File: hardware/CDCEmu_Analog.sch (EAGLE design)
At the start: 72 parts, among them J1 Audio In, J2 Audio Out, J3 Mic In, Q1 PCH, Q10 NPN, Q2 NCH, Q3 NCH, Q4 PCH, Q5 NCH, Q6 NPN, Q7 NPN, Q8 NPN, Q9 NPN, U1 1117, U2 BK8000L, U3 LM358, U4 NE5532

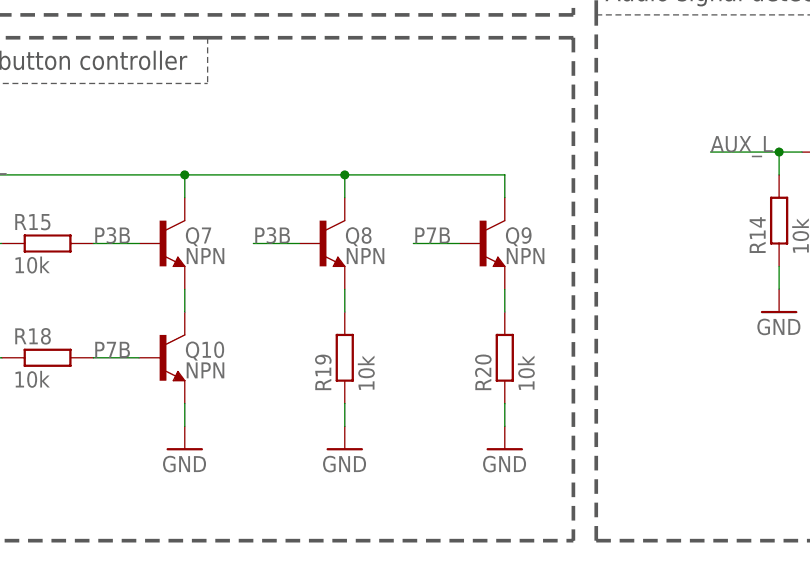
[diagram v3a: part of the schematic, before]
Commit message: [HW/Analog] Correct Vol+/- control transistors
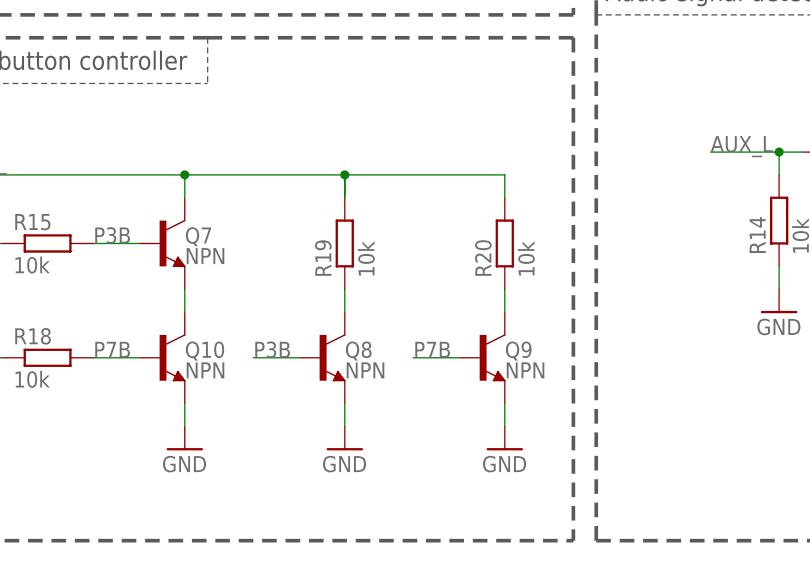
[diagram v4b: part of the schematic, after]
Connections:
- removed net Q7E: Q8.E, R19.2
- removed net Q8E: Q9.E, R20.2
- new net Q8C: Q8.C, R19.1
- new net Q9C: Q9.C, R20.1
- net CTRL: now also R19.2, R20.2; no longer Q8.C, Q9.C
- net GND: now also Q8.E, Q9.E; no longer R19.1, R20.1
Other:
- moved on the sheet: Q8, Q9, R19, R20
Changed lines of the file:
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@@
 <attribute name="VALUE" x="208.28" y="7.874" size="1.778" layer="96" font="vector"/>
 </instance>
-<instance part="Q8" gate="G$1" x="223.52" y="22.86" smashed="yes">
-<attribute name="NAME" x="226.06" y="22.86" size="1.778" layer="95" font="vector"/>
-<attribute name="VALUE" x="226.06" y="20.574" size="1.778" layer="96" font="vector"/>
-</instance>
-<instance part="Q9" gate="G$1" x="241.3" y="22.86" smashed="yes">
-<attribute name="NAME" x="243.84" y="22.86" size="1.778" layer="95" font="vector"/>
-<attribute name="VALUE" x="243.84" y="20.574" size="1.778" layer="96" font="vector"/>
+<instance part="Q8" gate="G$1" x="223.52" y="10.16" smashed="yes">
+<attribute name="NAME" x="226.06" y="10.16" size="1.778" layer="95" font="vector"/>
+<attribute name="VALUE" x="226.06" y="7.874" size="1.778" layer="96" font="vector"/>
+</instance>
+<instance part="Q9" gate="G$1" x="241.3" y="10.16" smashed="yes">
+<attribute name="NAME" x="243.84" y="10.16" size="1.778" layer="95" font="vector"/>
+<attribute name="VALUE" x="243.84" y="7.874" size="1.778" layer="96" font="vector"/>
 </instance>
 <instance part="R18" gate="G$1" x="193.04" y="10.16" smashed="yes">
@@
 <attribute name="VALUE" x="189.23" y="19.558" size="1.778" layer="96"/>
 </instance>
-<instance part="R19" gate="G$1" x="226.06" y="10.16" smashed="yes" rot="R90">
-<attribute name="NAME" x="224.5614" y="6.35" size="1.778" layer="95" rot="R90"/>
-<attribute name="VALUE" x="229.362" y="6.35" size="1.778" layer="96" rot="R90"/>
-</instance>
-<instance part="R20" gate="G$1" x="243.84" y="10.16" smashed="yes" rot="R90">
-<attribute name="NAME" x="242.3414" y="6.35" size="1.778" layer="95" rot="R90"/>
-<attribute name="VALUE" x="247.142" y="6.35" size="1.778" layer="96" rot="R90"/>
+<instance part="R19" gate="G$1" x="226.06" y="22.86" smashed="yes" rot="R90">
+<attribute name="NAME" x="224.5614" y="19.05" size="1.778" layer="95" rot="R90"/>
+<attribute name="VALUE" x="229.362" y="19.05" size="1.778" layer="96" rot="R90"/>
+</instance>
+<instance part="R20" gate="G$1" x="243.84" y="22.86" smashed="yes" rot="R90">
+<attribute name="NAME" x="242.3414" y="19.05" size="1.778" layer="95" rot="R90"/>
+<attribute name="VALUE" x="247.142" y="19.05" size="1.778" layer="96" rot="R90"/>
 </instance>
 <instance part="GND17" gate="1" x="208.28" y="0" smashed="yes">
@@
 </segment>
 <segment>
-<pinref part="R19" gate="G$1" pin="1"/>
-<wire x1="226.06" y1="5.08" x2="226.06" y2="2.54" width="0.1524" layer="91"/>
-<pinref part="GND18" gate="1" pin="GND"/>
-</segment>
-<segment>
-<pinref part="R20" gate="G$1" pin="1"/>
-<wire x1="243.84" y1="5.08" x2="243.84" y2="2.54" width="0.1524" layer="91"/>
-<pinref part="GND19" gate="1" pin="GND"/>
-</segment>
-<segment>
 <pinref part="C2" gate="G$1" pin="-"/>
 <wire x1="165.1" y1="86.36" x2="165.1" y2="83.82" width="0.1524" layer="91"/>
@@
 <pinref part="GND28" gate="1" pin="GND"/>
 </segment>
+<segment>
+<pinref part="Q8" gate="G$1" pin="E"/>
+<pinref part="GND18" gate="1" pin="GND"/>
+<wire x1="226.06" y1="5.08" x2="226.06" y2="2.54" width="0.1524" layer="91"/>
+</segment>
+<segment>
+<pinref part="Q9" gate="G$1" pin="E"/>
+<pinref part="GND19" gate="1" pin="GND"/>
+<wire x1="243.84" y1="5.08" x2="243.84" y2="2.54" width="0.1524" layer="91"/>
+</segment>
 </net>
 <net name="RX" class="0">
@@
 <label x="182.88" y="30.48" size="1.778" layer="95"/>
 <wire x1="208.28" y1="30.48" x2="226.06" y2="30.48" width="0.1524" layer="91"/>
-<pinref part="Q8" gate="G$1" pin="C"/>
-<wire x1="226.06" y1="30.48" x2="226.06" y2="27.94" width="0.1524" layer="91"/>
 <wire x1="226.06" y1="30.48" x2="243.84" y2="30.48" width="0.1524" layer="91"/>
-<pinref part="Q9" gate="G$1" pin="C"/>
-<wire x1="243.84" y1="30.48" x2="243.84" y2="27.94" width="0.1524" layer="91"/>
 <junction x="208.28" y="30.48"/>
 <junction x="226.06" y="30.48"/>
+<wire x1="226.06" y1="30.48" x2="226.06" y2="28.0924" width="0.1524" layer="91"/>
+<pinref part="R19" gate="G$1" pin="2"/>
+<wire x1="226.06" y1="27.94" x2="226.06" y2="30.48" width="0.1524" layer="91"/>
+<pinref part="R20" gate="G$1" pin="2"/>
+<wire x1="243.84" y1="30.48" x2="243.84" y2="27.94" width="0.1524" layer="91"/>
 </segment>
 <segment>
@@
 </segment>
 </net>
-<net name="Q7E" class="0">
-<segment>
-<pinref part="R19" gate="G$1" pin="2"/>
-<pinref part="Q8" gate="G$1" pin="E"/>
-<wire x1="226.06" y1="15.24" x2="226.06" y2="17.78" width="0.1524" layer="91"/>
-</segment>
-</net>
-<net name="Q8E" class="0">
-<segment>
-<pinref part="Q9" gate="G$1" pin="E"/>
-<pinref part="R20" gate="G$1" pin="2"/>
-<wire x1="243.84" y1="17.78" x2="243.84" y2="15.24" width="0.1524" layer="91"/>
-</segment>
-</net>
 <net name="P7B" class="0">
 <segment>
@@
 <segment>
 <pinref part="Q9" gate="G$1" pin="B"/>
-<wire x1="233.68" y1="22.86" x2="238.76" y2="22.86" width="0.1524" layer="91"/>
-<label x="233.68" y="22.86" size="1.778" layer="95"/>
+<wire x1="233.68" y1="10.16" x2="238.76" y2="10.16" width="0.1524" layer="91"/>
+<label x="233.68" y="10.16" size="1.778" layer="95"/>
 </segment>
 </net>
@@
 <segment>
 <pinref part="Q8" gate="G$1" pin="B"/>
-<wire x1="215.9" y1="22.86" x2="220.98" y2="22.86" width="0.1524" layer="91"/>
-<label x="215.9" y="22.86" size="1.778" layer="95"/>
+<wire x1="215.9" y1="10.16" x2="220.98" y2="10.16" width="0.1524" layer="91"/>
+<label x="215.9" y="10.16" size="1.778" layer="95"/>
 </segment>
 </net>
@@
 </segment>
 </net>
+<net name="Q8C" class="0">
+<segment>
+<pinref part="R19" gate="G$1" pin="1"/>
+<pinref part="Q8" gate="G$1" pin="C"/>
+<wire x1="226.06" y1="17.78" x2="226.06" y2="15.24" width="0.1524" layer="91"/>
+</segment>
+</net>
+<net name="Q9C" class="0">
+<segment>
+<pinref part="R20" gate="G$1" pin="1"/>
+<pinref part="Q9" gate="G$1" pin="C"/>
+<wire x1="243.84" y1="17.78" x2="243.84" y2="15.24" width="0.1524" layer="91"/>
+</segment>
+</net>
